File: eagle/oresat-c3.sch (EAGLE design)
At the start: 160 parts, among them J1 J-SAMTEC-TFM-110-X1-XXX-D-RA, J10 U.FL, J11 U.FL, J13 U.FL, J14 U.FL, J15 HARWIN-2X8X1.27, J19 HARWIN-2X8X1.27, J2 U.FL, J3 U.FL, J4 U.FL, J5 2-1734592-0, J6 J-SAMTEC-TFM-120-X1-XXX-D-RA, J8 U.FL, J9 U.FL, Q1 MOSFET-PCH-SOT23-6, U1 MAX892LEUA+T21-0036K-L, U11 U-ONSEMI-AX5043, U12 LP2985XX-N, U13 U-ONSEMI-AX5043, U14 LP2985XX-N, U2 TCAN330, U3 TCAN330, U4 TPS259621 - eFuse, U5 TPS62111RSA, U6 MAX6374KA-T21-0078H-L, U7 STM32F446RE, U9 SFEM016GB1EM1TO-A-HG-111-STD, X1 16MHZ-2.5x2mm, X3 TAITIEN-TY, X4 TAITIEN-TY

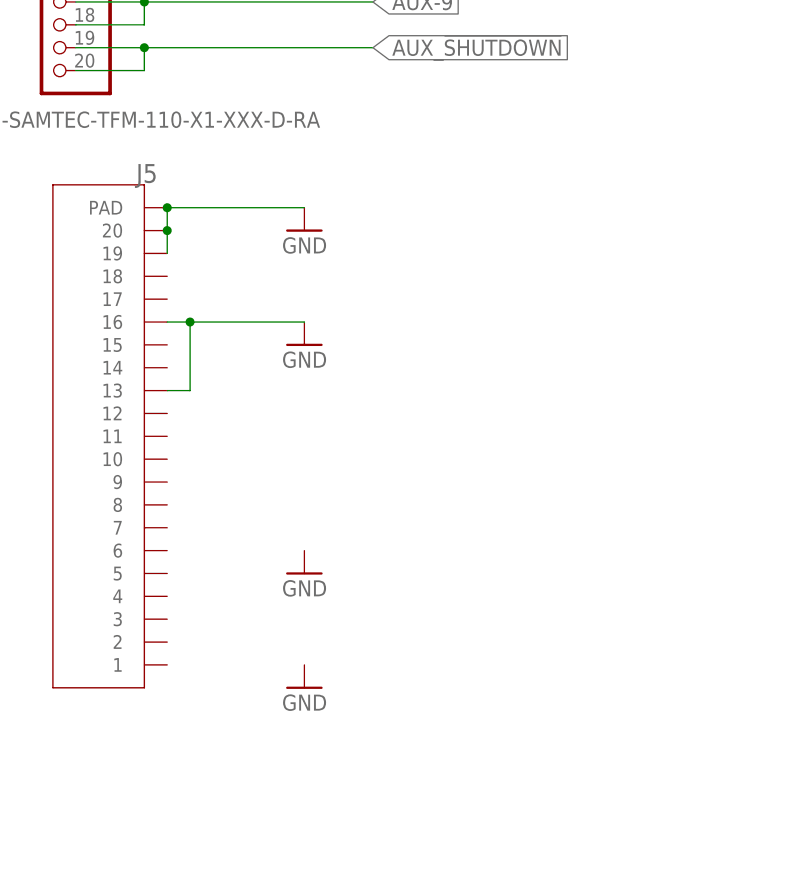
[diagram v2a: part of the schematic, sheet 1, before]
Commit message: Adding in Jumper and completed more of the routing
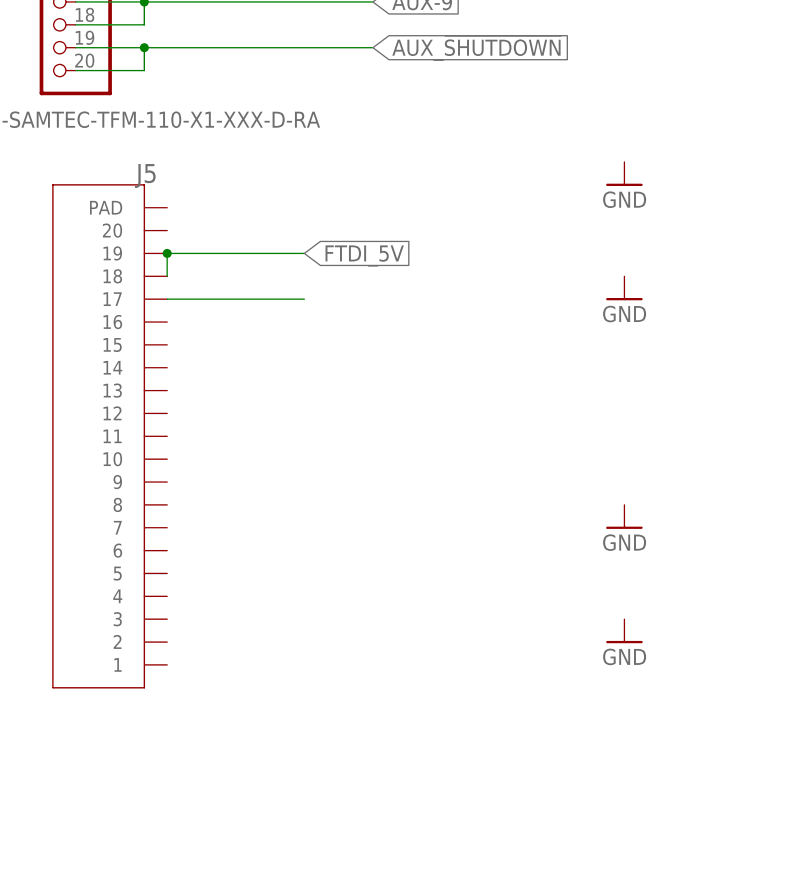
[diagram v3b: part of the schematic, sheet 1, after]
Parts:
- added JP1: (no value), pinhead:PINHD-1X2
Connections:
- new net FTDI_5V: J5.18, J5.19, JP1.2
- new net N$6: J5.17
- net GND: no longer J5.13, J5.16, J5.19, J5.20, J5.PAD
- net VBUSP: now also JP1.1
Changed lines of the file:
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@@
 <part name="GND59" library="supply1" library_urn="urn:adsk.eagle:library:371" deviceset="GND" device=""/>
 <part name="D6" library="D-LittelFuse-Uni-Directional-TVS" deviceset="SZ1SMB5.0AT3G" device="" package3d_urn="urn:adsk.eagle:package:17409861/1"/>
+<part name="JP1" library="pinhead" library_urn="urn:adsk.eagle:library:325" deviceset="PINHD-1X2" device="" package3d_urn="urn:adsk.eagle:package:22435/2"/>
+<part name="VBUSP3" library="oresat-supplies" deviceset="VBUSP" device=""/>
 </parts>
 <sheets>
@@
 <attribute name="NAME" x="29.5656" y="84.0486" size="2.0828" layer="95" ratio="6" rot="SR0"/>
 </instance>
-<instance part="GND6" gate="1" x="48.26" y="78.74" smashed="yes" rot="MR0">
-<attribute name="VALUE" x="50.8" y="76.2" size="1.778" layer="96" rot="MR0"/>
+<instance part="GND6" gate="1" x="83.82" y="83.82" smashed="yes" rot="MR0">
+<attribute name="VALUE" x="86.36" y="81.28" size="1.778" layer="96" rot="MR0"/>
 </instance>
-<instance part="GND13" gate="1" x="48.26" y="66.04" smashed="yes" rot="MR0">
-<attribute name="VALUE" x="50.8" y="63.5" size="1.778" layer="96" rot="MR0"/>
+<instance part="GND13" gate="1" x="83.82" y="71.12" smashed="yes" rot="MR0">
+<attribute name="VALUE" x="86.36" y="68.58" size="1.778" layer="96" rot="MR0"/>
 </instance>
-<instance part="GND38" gate="1" x="48.26" y="40.64" smashed="yes" rot="MR0">
-<attribute name="VALUE" x="50.8" y="38.1" size="1.778" layer="96" rot="MR0"/>
+<instance part="GND38" gate="1" x="83.82" y="45.72" smashed="yes" rot="MR0">
+<attribute name="VALUE" x="86.36" y="43.18" size="1.778" layer="96" rot="MR0"/>
 </instance>
-<instance part="GND58" gate="1" x="48.26" y="27.94" smashed="yes" rot="MR0">
-<attribute name="VALUE" x="50.8" y="25.4" size="1.778" layer="96" rot="MR0"/>
+<instance part="GND58" gate="1" x="83.82" y="33.02" smashed="yes" rot="MR0">
+<attribute name="VALUE" x="86.36" y="30.48" size="1.778" layer="96" rot="MR0"/>
 </instance>
 </instances>
@@
 <wire x1="30.48" y1="190.5" x2="58.42" y2="190.5" width="0.1524" layer="91"/>
 </segment>
-<segment>
-<pinref part="J5" gate="G$1" pin="PAD"/>
-<wire x1="33.02" y1="81.28" x2="48.26" y2="81.28" width="0.1524" layer="91"/>
-<pinref part="GND6" gate="1" pin="GND"/>
-<pinref part="J5" gate="G$1" pin="19"/>
-<pinref part="J5" gate="G$1" pin="20"/>
-<wire x1="33.02" y1="76.2" x2="33.02" y2="78.74" width="0.1524" layer="91"/>
-<wire x1="33.02" y1="78.74" x2="33.02" y2="81.28" width="0.1524" layer="91"/>
-<junction x="33.02" y="78.74"/>
-<junction x="33.02" y="81.28"/>
-</segment>
-<segment>
-<pinref part="J5" gate="G$1" pin="16"/>
-<pinref part="GND13" gate="1" pin="GND"/>
-<wire x1="33.02" y1="68.58" x2="35.56" y2="68.58" width="0.1524" layer="91"/>
-<pinref part="J5" gate="G$1" pin="13"/>
-<wire x1="35.56" y1="68.58" x2="48.26" y2="68.58" width="0.1524" layer="91"/>
-<wire x1="33.02" y1="60.96" x2="35.56" y2="60.96" width="0.1524" layer="91"/>
-<wire x1="35.56" y1="60.96" x2="35.56" y2="68.58" width="0.1524" layer="91"/>
-<junction x="35.56" y="68.58"/>
-</segment>
 </net>
 <net name="OPD_SDA" class="0">
@@
 </segment>
 </net>
+<net name="FTDI_5V" class="0">
+<segment>
+<pinref part="J5" gate="G$1" pin="19"/>
+<wire x1="33.02" y1="76.2" x2="48.26" y2="76.2" width="0.1524" layer="91"/>
+<pinref part="J5" gate="G$1" pin="18"/>
+<wire x1="33.02" y1="73.66" x2="33.02" y2="76.2" width="0.1524" layer="91"/>
+<junction x="33.02" y="76.2"/>
+<label x="48.26" y="76.2" size="1.778" layer="95" xref="yes"/>
+</segment>
+</net>
+<net name="N$6" class="0">
+<segment>
+<pinref part="J5" gate="G$1" pin="17"/>
+<wire x1="33.02" y1="71.12" x2="48.26" y2="71.12" width="0.1524" layer="91"/>
+</segment>
+</net>
 </nets>
 </sheet>
@@
 <text x="332.74" y="264.16" size="3.81" layer="97">Watchdog</text>
 <wire x1="302.26" y1="180.34" x2="302.26" y2="160.02" width="0.1524" layer="97"/>
-<text x="96.52" y="160.02" size="1.778" layer="97">Internal Pull-up Resistor at MCU</text>
+<text x="73.66" y="160.02" size="1.778" layer="97">Internal Pull-up Resistor at MCU</text>
 <wire x1="302.26" y1="180.34" x2="261.62" y2="180.34" width="0.1524" layer="97"/>
 <wire x1="261.62" y1="180.34" x2="261.62" y2="200.66" width="0.1524" layer="97"/>
@@
 <attribute name="VALUE" x="402.59" y="127" size="1.778" layer="96" rot="R270"/>
 </instance>
+<instance part="JP1" gate="G$1" x="86.36" y="177.8" smashed="yes">
+<attribute name="NAME" x="80.01" y="183.515" size="1.778" layer="95"/>
+<attribute name="VALUE" x="80.01" y="172.72" size="1.778" layer="96"/>
+</instance>
+<instance part="VBUSP3" gate="G$1" x="76.2" y="187.96" smashed="yes">
+<attribute name="VALUE" x="76.2" y="190.754" size="1.778" layer="96" align="bottom-center"/>
+</instance>
 </instances>
 <busses>
@@
 <segment>
 <wire x1="190.5" y1="116.84" x2="162.56" y2="116.84" width="0.1524" layer="91"/>
-<wire x1="162.56" y1="116.84" x2="162.56" y2="162.56" width="0.1524" layer="91"/>
+<wire x1="162.56" y1="116.84" x2="162.56" y2="165.1" width="0.1524" layer="91"/>
 <label x="190.5" y="116.84" size="1.778" layer="95" rot="MR0"/>
-<label x="78.74" y="162.56" size="1.778" layer="95"/>
+<label x="71.12" y="165.1" size="1.778" layer="95" rot="R180" xref="yes"/>
 <pinref part="U7" gate="G$1" pin="PA2"/>
-<wire x1="162.56" y1="162.56" x2="71.12" y2="162.56" width="0.1524" layer="91"/>
+<wire x1="162.56" y1="165.1" x2="71.12" y2="165.1" width="0.1524" layer="91"/>
 </segment>
 </net>
@@
 <wire x1="190.5" y1="114.3" x2="165.1" y2="114.3" width="0.1524" layer="91"/>
 <label x="190.5" y="114.3" size="1.778" layer="95" rot="MR0"/>
-<label x="78.74" y="160.02" size="1.778" layer="95"/>
+<label x="71.12" y="160.02" size="1.778" layer="95" rot="R180" xref="yes"/>
 <pinref part="U7" gate="G$1" pin="PA3"/>
 <wire x1="71.12" y1="160.02" x2="165.1" y2="160.02" width="0.1524" layer="91"/>
@@
 <junction x="177.8" y="139.7"/>
 <wire x1="177.8" y1="137.16" x2="172.72" y2="137.16" width="0.1524" layer="91"/>
+<label x="144.78" y="175.26" size="1.778" layer="95" rot="R180" xref="yes"/>
 </segment>
 </net>
@@
 <wire x1="167.64" y1="190.5" x2="144.78" y2="190.5" width="0.1524" layer="91"/>
 <pinref part="U7" gate="G$1" pin="PA14"/>
+<label x="144.78" y="190.5" size="1.778" layer="95" rot="R180" xref="yes"/>
 </segment>
 </net>
@@
 <wire x1="170.18" y1="195.58" x2="144.78" y2="195.58" width="0.1524" layer="91"/>
 <pinref part="U7" gate="G$1" pin="PA13"/>
+<label x="144.78" y="195.58" size="1.778" layer="95" rot="R180" xref="yes"/>
 </segment>
 </net>
@@
 </segment>
 </net>
+<net name="VBUSP" class="0">
+<segment>
+<pinref part="JP1" gate="G$1" pin="1"/>
+<wire x1="83.82" y1="180.34" x2="76.2" y2="180.34" width="0.1524" layer="91"/>
+<wire x1="76.2" y1="180.34" x2="76.2" y2="187.96" width="0.1524" layer="91"/>
+<pinref part="VBUSP3" gate="G$1" pin="VBUSP"/>
+</segment>
+</net>
+<net name="FTDI_5V" class="0">
+<segment>
+<pinref part="JP1" gate="G$1" pin="2"/>
+<wire x1="83.82" y1="177.8" x2="71.12" y2="177.8" width="0.1524" layer="91"/>
+<label x="71.12" y="177.8" size="1.778" layer="95" rot="R180" xref="yes"/>
+</segment>
+</net>

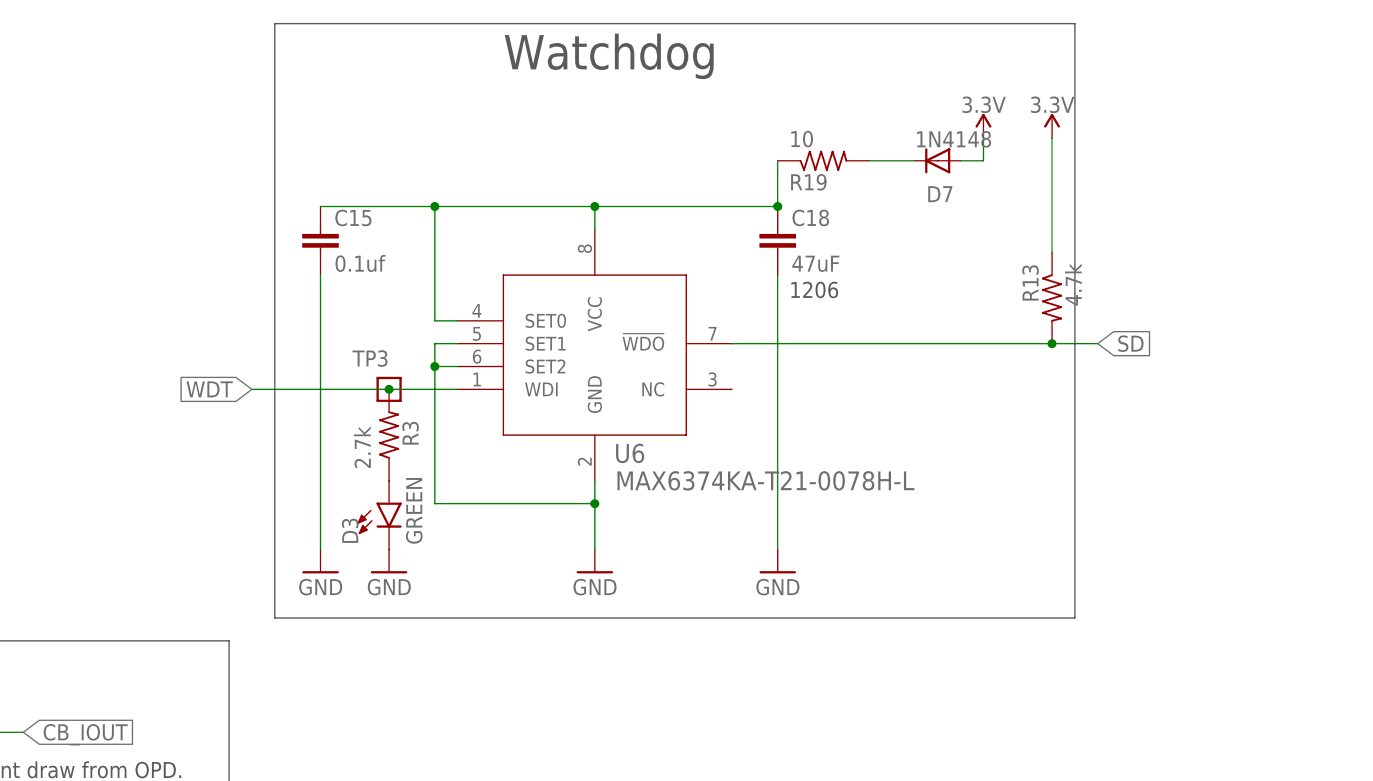
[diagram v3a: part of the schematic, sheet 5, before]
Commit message: Wired in the edge connector and added the data sheet for the littlefuse TVS diode
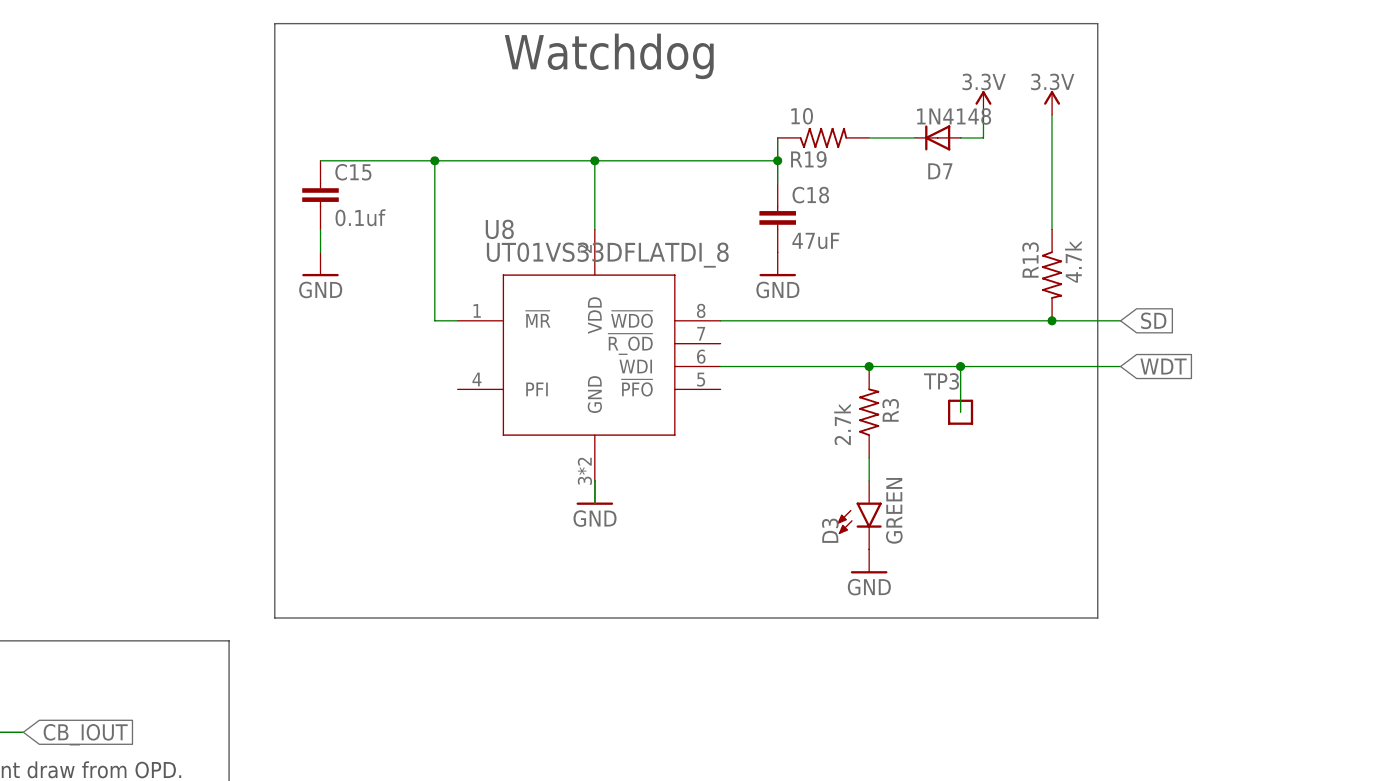
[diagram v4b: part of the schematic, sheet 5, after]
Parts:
- removed U6: MAX6374KA-T21-0078H-L, U-Maxim-MAX6374-watchdog:MAX6374KA-T21-0078H-L
- added U8: UT01VS33DFLATDI_8, U-COBHAM-UT01VS33D-Voltage-Supervisor:UT01VS33DFLATDI_8
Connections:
- removed net N$6: J5.17
- new net HOST_D+: J5.3
- new net HOST_D-: J5.2
- new net SLAVE_D+: J5.5
- new net SLAVE_D-: J5.4
- new net SWD: J5.6
- net 3.3V: now also J5.15, J5.16
- net GND: now also J5.1, J5.11, J5.14, J5.17, J5.20, J5.7, J5.PAD, U8.GND; no longer U6.GND, U6.SET1, U6.SET2
- net NRST: now also J5.8
- net SD: now also U8.!WDO; no longer U6.!WDO
- net SWCLK: now also J5.9
- net SWDIO: now also J5.10
- net USART2_RX: now also J5.12
- net USART2_TX: now also J5.13
- net WDT: now also U8.WDI; no longer U6.WDI
- net WDT-PWR: now also U8.!MR, U8.VDD; no longer U6.SET0, U6.VCC
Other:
- note removed: "1206"
- moved on the sheet: C15, C18, D3, D7, R13, R19, R3, TP3
